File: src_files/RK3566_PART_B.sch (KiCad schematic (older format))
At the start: 1 part

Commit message: wifi module complete
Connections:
- net eMMC_D1_FLASH_D1: now also U?.B27 (EMMC_D1)
- net eMMC_D2_FLASH_D2: now also U?.B32 (EMMC_D2)
- net SDMMC1_D3: now reaches U?.1A20 (SDMMC1_D3)
- net I2S2_SDO_M0: now reaches U?.1B20 (I2S2_LRCK_TX_M0)
- net SDMMC1_D0: now reaches U?.1C19 (SDMMC1_D0)
- net UART1_RX_M0: now reaches U?.1C20 (UART1_RX_M0)
- net SDMMC1_D2: now reaches U?.1D18 (SDMMC1_D2)
- net I2S2_LRCK_TX_M0: now reaches U?.1D19 (I2S2_LRCK_TX_M0)
- net SDMMC1_D1: now reaches U?.1E18 (SDMMC1_D1)
- net WIFI_REG_ON_H_GPIO2_B1: now reaches U?.A35 (SDMMC1_PWREN)
- net BT_WAKE_HOST_H_GPIO2_C0: now reaches U?.A37 (I2S2_LRCK_RX_M0)
- net WIFI_WAKE_HOST_H_GPIO2_B2: now reaches U?.B34 (SDMMC1_DET)
- net SDMMC1_CMD: now reaches U?.B35 (SDMMC1_CMD)
- net HOST_WAKE_BT_H_GPIO2_C1: now reaches U?.B36 (I2S2_MCLK_M0)
- net SDMMC1_CLK: now reaches U?.B37 (SDMMC1_CLK)
- net CLK32K_OUT1_WIFI: now reaches U?.B38 (CLK32K_OUT1)
- net I2S2_SCLK_TX_M0: now reaches U?.C37 (I2S2_SCLK_TX_M0)
- net I2S2_SDI_M0: now reaches U?.D37 (I2S2_SDI_M0)
- net BT_REG_ON_H_GPIO2_B7: now reaches U?.D38 (I2S2_SCLK_RX_M0)
- net UART1_RTSn_M0: now reaches U?.F37 (UART1_RTSn_M0)
- net UART1_TX_M0: now reaches U?.F38 (UART1_TX_M0)
- net UART1_CTSn_M0: now reaches U?.G37 (UART1_CTSn_M0)
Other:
- note added: "RK3566 TO WIFI/BT MODULE"
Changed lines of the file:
@@
 $Descr A3 16535 11693
 encoding utf-8
-Sheet 6 7
+Sheet 5 8
 Title ""
 Date ""
@@
 Text HLabel 3750 2025 0    33   Input ~ 0
 eMMC_CMD_FLASH_WRn
+Wire Wire Line
+	4025 1275 3750 1275
+Wire Wire Line
+	3750 1375 4025 1375
+Text HLabel 8250 1175 2    39   Input ~ 0
+SDMMC1_D0
+Text HLabel 8250 1275 2    39   Input ~ 0
+SDMMC1_D1
+Text HLabel 8250 1375 2    39   Input ~ 0
+SDMMC1_D2
+Text HLabel 8250 1475 2    39   Input ~ 0
+SDMMC1_D3
+Text HLabel 8250 1625 2    39   Input ~ 0
+SDMMC1_CMD
+Text HLabel 8250 1725 2    39   Input ~ 0
+SDMMC1_CLK
+Text HLabel 8250 1875 2    39   Input ~ 0
+WIFI_REG_ON_H_GPIO2_B1
+Text HLabel 8250 1975 2    39   Input ~ 0
+WIFI_WAKE_HOST_H_GPIO2_B2
+Wire Wire Line
+	8075 1175 8250 1175
+Wire Wire Line
+	8075 1275 8250 1275
+Wire Wire Line
+	8075 1375 8250 1375
+Wire Wire Line
+	8075 1475 8250 1475
+Wire Wire Line
+	8075 1625 8250 1625
+Wire Wire Line
+	8075 1725 8250 1725
+Wire Wire Line
+	8075 1875 8250 1875
+Wire Wire Line
+	8075 1975 8250 1975
+Text HLabel 8250 2175 2    39   Input ~ 0
+UART1_RX_M0
+Wire Wire Line
+	8075 2175 8250 2175
+Text HLabel 8250 2275 2    39   Input ~ 0
+UART1_TX_M0
+Wire Wire Line
+	8075 2275 8250 2275
+Text HLabel 8250 2375 2    39   Input ~ 0
+UART1_RTSn_M0
+Wire Wire Line
+	8075 2375 8250 2375
+Text HLabel 8250 2475 2    39   Input ~ 0
+UART1_CTSn_M0
+Wire Wire Line
+	8075 2475 8250 2475
+Text HLabel 8250 2625 2    39   Input ~ 0
+BT_REG_ON_H_GPIO2_B7
+Wire Wire Line
+	8075 2625 8250 2625
+Text HLabel 8250 2725 2    39   Input ~ 0
+BT_WAKE_HOST_H_GPIO2_C0
+Wire Wire Line
+	8075 2725 8250 2725
+Text HLabel 8250 2825 2    39   Input ~ 0
+HOST_WAKE_BT_H_GPIO2_C1
+Wire Wire Line
+	8075 2825 8250 2825
+Text HLabel 8250 2975 2    39   Input ~ 0
+I2S2_SCLK_TX_M0
+Wire Wire Line
+	8075 2975 8250 2975
+Text HLabel 8250 3075 2    39   Input ~ 0
+I2S2_LRCK_TX_M0
+Wire Wire Line
+	8075 3075 8250 3075
+Text HLabel 8250 3175 2    39   Input ~ 0
+I2S2_SDO_M0
+Wire Wire Line
+	8075 3175 8250 3175
+Text HLabel 8250 3275 2    39   Input ~ 0
+I2S2_SDI_M0
+Wire Wire Line
+	8075 3275 8250 3275
+Text HLabel 8250 3475 2    39   Input ~ 0
+CLK32K_OUT1_WIFI
+Wire Wire Line
+	8075 3475 8250 3475
+Wire Notes Line
+	8050 1050 9425 1050
+Wire Notes Line
+	9425 1050 9425 1750
+Text Notes 9475 2850 1    50   ~ 10
+RK3566 TO WIFI/BT MODULE
+Wire Notes Line
+	8075 3550 9450 3550
+Wire Notes Line
+	9450 3550 9450 2850
 $EndSCHEMATC

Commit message: sata updated
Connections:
- net SATA1_RX-: now reaches U?.V37 (USB3_HOST1_SSRXn/SATA1_RXn)
- net SATA1_RX+: now reaches U?.V38 (USB3_HOST1_SSRXp/SATA1_RXp)
- net SATA1_TX+: now reaches U?.W37 (USB3_HOST1_SSTXp/SATA1_TXp)
- net SATA1_TX-: now reaches U?.W38 (USB3_HOST1_SSTXn/SATA1_TXn)
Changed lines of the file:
@@
 Wire Notes Line
 	9450 3550 9450 2850
+Text HLabel 3900 5275 0    30   Input ~ 0
+SATA1_TX+
+Text HLabel 3900 5375 0    30   Input ~ 0
+SATA1_TX-
+Wire Wire Line
+	4025 5275 3900 5275
+Wire Wire Line
+	3900 5375 4025 5375
+Text HLabel 3900 5525 0    30   Input ~ 0
+SATA1_RX+
+Text HLabel 3900 5625 0    30   Input ~ 0
+SATA1_RX-
+Wire Wire Line
+	4025 5525 3900 5525
+Wire Wire Line
+	3900 5625 4025 5625
 $EndSCHEMATC

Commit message: littleupdate
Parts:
- U1: renamed from U?; footprint (none) -> greencharge-footprints:BGA828C65P31X31_2100X2100X161N
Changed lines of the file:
@@
 $Descr A3 16535 11693
 encoding utf-8
-Sheet 5 11
+Sheet 4 11
 Title ""
 Date ""
@@
 P 6025 575
 AR Path="/62988BD1" Ref="U?"  Part="3"
-AR Path="/62987DE9/62988BD1" Ref="U?"  Part="3"
-F 0 "U?" H 6050 240 50  0000 C CNN
+AR Path="/62987DE9/62988BD1" Ref="U1"  Part="3"
+F 0 "U1" H 6050 240 50  0000 C CNN
 F 1 "RK3566" H 6050 149 50  0000 C CNN
-F 2 "" H 5475 475 50  0001 C CNN
+F 2 "greencharge-footprints:BGA828C65P31X31_2100X2100X161N" H 5475 475 50  0001 C CNN
 F 3 "" H 5475 475 50  0001 C CNN
 	3    6025 575

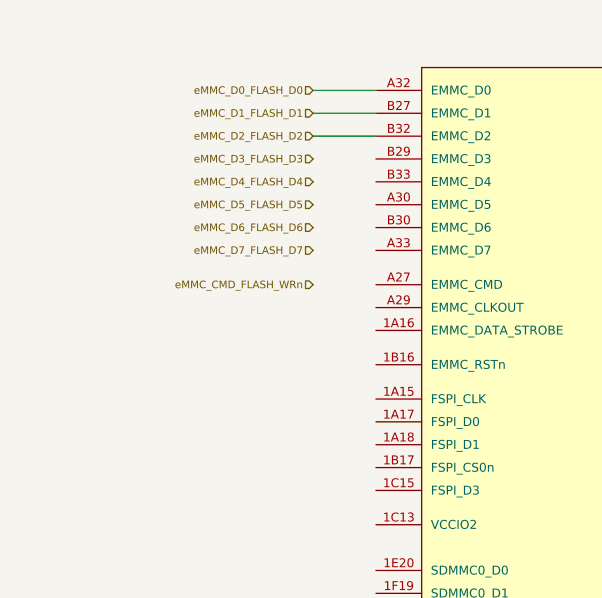
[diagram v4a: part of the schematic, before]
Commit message: added 3 screens
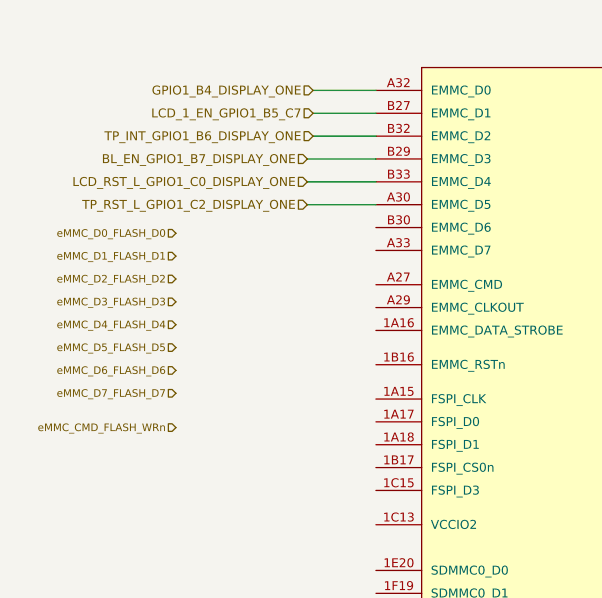
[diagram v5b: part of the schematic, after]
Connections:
- net eMMC_D0_FLASH_D0: no longer U1.A32 (EMMC_D0)
- net eMMC_D1_FLASH_D1: no longer U1.B27 (EMMC_D1)
- net eMMC_D2_FLASH_D2: no longer U1.B32 (EMMC_D2)
- net TP_RST_L_GPIO1_C2_DISPLAY_ONE: now reaches U1.A30 (EMMC_D5)
- net BL_EN_GPIO1_B7_DISPLAY_ONE: now reaches U1.B29 (EMMC_D3)
- net LCD_RST_L_GPIO1_C0_DISPLAY_ONE: now reaches U1.B33 (EMMC_D4)
- new net GPIO1_B4_DISPLAY_ONE: U1.A32 (EMMC_D0)
- new net LCD_1_EN_GPIO1_B5_C7: U1.B27 (EMMC_D1)
- new net TP_INT_GPIO1_B6_DISPLAY_ONE: U1.B32 (EMMC_D2)
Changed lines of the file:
@@
 	1    0    0    -1
 $EndComp
-Text HLabel 3750 1175 0    33   Input ~ 0
-eMMC_D0_FLASH_D0
-Wire Wire Line
-	4025 1175 3750 1175
-Text HLabel 3750 1275 0    33   Input ~ 0
-eMMC_D1_FLASH_D1
-Text HLabel 3750 1375 0    33   Input ~ 0
-eMMC_D2_FLASH_D2
-Text HLabel 3750 1475 0    33   Input ~ 0
-eMMC_D3_FLASH_D3
-Text HLabel 3750 1575 0    33   Input ~ 0
-eMMC_D4_FLASH_D4
-Text HLabel 3750 1675 0    33   Input ~ 0
-eMMC_D5_FLASH_D5
-Text HLabel 3750 1775 0    33   Input ~ 0
-eMMC_D6_FLASH_D6
-Text HLabel 3750 1875 0    33   Input ~ 0
-eMMC_D7_FLASH_D7
-Text HLabel 3750 2025 0    33   Input ~ 0
-eMMC_CMD_FLASH_WRn
-Wire Wire Line
-	4025 1275 3750 1275
-Wire Wire Line
-	3750 1375 4025 1375
 Text HLabel 8250 1175 2    39   Input ~ 0
 SDMMC1_D0
@@
 Wire Wire Line
 	3900 5625 4025 5625
+Wire Wire Line
+	3750 1375 4025 1375
+Wire Wire Line
+	4025 1275 3750 1275
+Text HLabel 3150 2650 0    33   Input ~ 0
+eMMC_CMD_FLASH_WRn
+Text HLabel 3150 2500 0    33   Input ~ 0
+eMMC_D7_FLASH_D7
+Text HLabel 3150 2400 0    33   Input ~ 0
+eMMC_D6_FLASH_D6
+Text HLabel 3150 2300 0    33   Input ~ 0
+eMMC_D5_FLASH_D5
+Text HLabel 3150 2200 0    33   Input ~ 0
+eMMC_D4_FLASH_D4
+Text HLabel 3150 2100 0    33   Input ~ 0
+eMMC_D3_FLASH_D3
+Text HLabel 3150 2000 0    33   Input ~ 0
+eMMC_D2_FLASH_D2
+Text HLabel 3150 1900 0    33   Input ~ 0
+eMMC_D1_FLASH_D1
+Wire Wire Line
+	4025 1175 3750 1175
+Text HLabel 3150 1800 0    33   Input ~ 0
+eMMC_D0_FLASH_D0
+Text HLabel 3750 1175 0    39   Input ~ 0
+GPIO1_B4_DISPLAY_ONE
+Text HLabel 3750 1275 0    39   Input ~ 0
+LCD_1_EN_GPIO1_B5_C7
+Text HLabel 3750 1375 0    39   Input ~ 0
+TP_INT_GPIO1_B6_DISPLAY_ONE
+Text HLabel 3725 1475 0    39   Input ~ 0
+BL_EN_GPIO1_B7_DISPLAY_ONE
+Wire Wire Line
+	4025 1475 3725 1475
+Text HLabel 3725 1575 0    39   Input ~ 0
+LCD_RST_L_GPIO1_C0_DISPLAY_ONE
+Text HLabel 3725 1675 0    39   Input ~ 0
+TP_RST_L_GPIO1_C2_DISPLAY_ONE
+Wire Wire Line
+	4025 1575 3725 1575
+Wire Wire Line
+	3725 1675 4025 1675
 $EndSCHEMATC

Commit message: all screens added_3 items left
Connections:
- net HDMITX_CEC_M0: now reaches U1.1V5 (HDMITX_CEC_M)
- net HDMITX_SDA: now reaches U1.AP11 (HDMITX_SDA)
- net HDMITX_SCL: now reaches U1.AR12 (HDMITX_SCL)
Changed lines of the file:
@@
 $Descr A3 16535 11693
 encoding utf-8
-Sheet 4 11
+Sheet 4 12
 Title ""
 Date ""
@@
 Comment4 ""
 $EndDescr
-$Comp
-L GCL_Integrated-Circuits:RK3566 U?
-U 3 1 62988BD1
-P 6025 575
-AR Path="/62988BD1" Ref="U?"  Part="3"
-AR Path="/62987DE9/62988BD1" Ref="U1"  Part="3"
-F 0 "U1" H 6050 240 50  0000 C CNN
-F 1 "RK3566" H 6050 149 50  0000 C CNN
-F 2 "greencharge-footprints:BGA828C65P31X31_2100X2100X161N" H 5475 475 50  0001 C CNN
-F 3 "" H 5475 475 50  0001 C CNN
-	3    6025 575
-	1    0    0    -1
-$EndComp
 Text HLabel 8250 1175 2    39   Input ~ 0
 SDMMC1_D0
@@
 Wire Wire Line
 	3725 1675 4025 1675
+Text HLabel 8325 4475 2    50   Input ~ 0
+HDMITX_CEC_M0
+$Comp
+L GCL_Integrated-Circuits:RK3566 U?
+U 3 1 62988BD1
+P 6025 575
+AR Path="/62988BD1" Ref="U?"  Part="3"
+AR Path="/62987DE9/62988BD1" Ref="U1"  Part="3"
+F 0 "U1" H 6050 240 50  0000 C CNN
+F 1 "RK3566" H 6050 149 50  0000 C CNN
+F 2 "greencharge-footprints:BGA828C65P31X31_2100X2100X161N" H 5475 475 50  0001 C CNN
+F 3 "" H 5475 475 50  0001 C CNN
+	3    6025 575
+	1    0    0    -1
+$EndComp
+Wire Wire Line
+	8075 4475 8325 4475
+Text HLabel 8325 4375 2    50   Input ~ 0
+HDMITX_SDA
+Text HLabel 8325 4275 2    50   Input ~ 0
+HDMITX_SCL
+Wire Wire Line
+	8075 4275 8325 4275
+Wire Wire Line
+	8075 4375 8325 4375
 $EndSCHEMATC

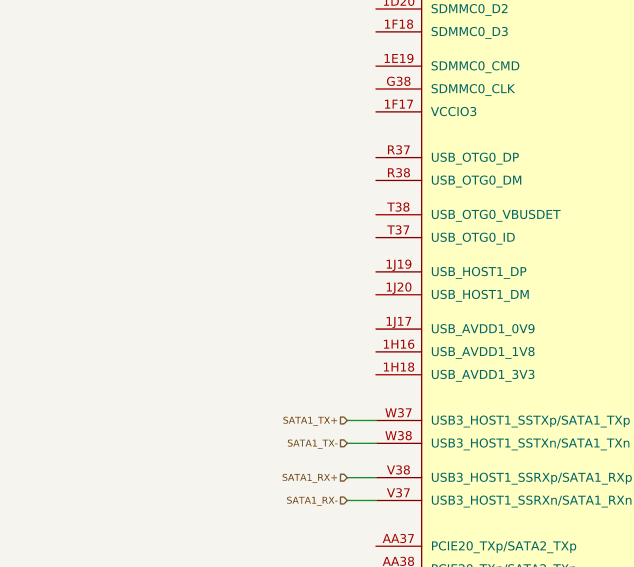
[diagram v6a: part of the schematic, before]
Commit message: updated 4G module and simcard
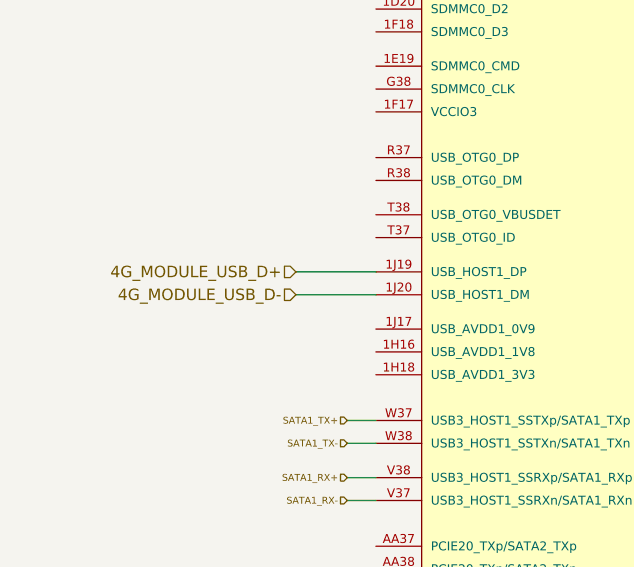
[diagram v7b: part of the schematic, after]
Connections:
- net 4G_MODULE_USB_D+: now reaches U1.1J19 (USB_HOST1_DP)
- net 4G_MODULE_USB_D-: now reaches U1.1J20 (USB_HOST1_DM)
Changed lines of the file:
@@
 $Descr A3 16535 11693
 encoding utf-8
-Sheet 4 12
+Sheet 4 13
 Title ""
 Date ""
@@
 Wire Wire Line
 	8075 4375 8325 4375
+Text HLabel 3675 4625 0    50   Input ~ 0
+4G_MODULE_USB_D+
+Text HLabel 3675 4725 0    50   Input ~ 0
+4G_MODULE_USB_D-
+Wire Wire Line
+	4025 4625 3675 4625
+Wire Wire Line
+	3675 4725 4025 4725
 $EndSCHEMATC

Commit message: update NFC, 5G, GPS__left LiPo charger+screen changes
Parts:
- added C?: 100nF, symbol Device:C_Small
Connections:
- net UART6_TX_M1: now reaches U1.1E20 (SDMMC0_D0)
- net VCCIO_SD: now reaches U1.1F17 (VCCIO3)
- net VCCIO_SD: now also C?.1
- net UART6_RX_M1: now reaches U1.1F19 (SDMMC0_D1)
- net I2C4_SDA_M0_TO_NFC_SCL: now reaches U1.AE2 (GPIO4_B3_d)
- net I2C4_SDA_M0_TO_NFC_SDA: now reaches U1.AF2 (GPIO4_B2_d)
- net GPIO4_B1_d_TO_NFC_REQ: now reaches U1.AG2 (GPIO4_B1_d)
- new net GND: C?.2
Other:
- note added: "SATA_INTERFACE\nZ=90 Ohms"
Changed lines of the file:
@@
 $Descr A3 16535 11693
 encoding utf-8
-Sheet 4 13
+Sheet 13 13
 Title ""
 Date ""
@@
 Wire Wire Line
 	4025 1275 3750 1275
-Text HLabel 3150 2650 0    33   Input ~ 0
-eMMC_CMD_FLASH_WRn
-Text HLabel 3150 2500 0    33   Input ~ 0
-eMMC_D7_FLASH_D7
-Text HLabel 3150 2400 0    33   Input ~ 0
-eMMC_D6_FLASH_D6
-Text HLabel 3150 2300 0    33   Input ~ 0
-eMMC_D5_FLASH_D5
-Text HLabel 3150 2200 0    33   Input ~ 0
-eMMC_D4_FLASH_D4
-Text HLabel 3150 2100 0    33   Input ~ 0
-eMMC_D3_FLASH_D3
-Text HLabel 3150 2000 0    33   Input ~ 0
-eMMC_D2_FLASH_D2
-Text HLabel 3150 1900 0    33   Input ~ 0
-eMMC_D1_FLASH_D1
 Wire Wire Line
 	4025 1175 3750 1175
-Text HLabel 3150 1800 0    33   Input ~ 0
-eMMC_D0_FLASH_D0
 Text HLabel 3750 1175 0    39   Input ~ 0
 GPIO1_B4_DISPLAY_ONE
@@
 Wire Wire Line
 	3675 4725 4025 4725
+Text HLabel 3850 3375 0    50   Input ~ 0
+UART6_RX_M1
+Text HLabel 3850 3275 0    50   Input ~ 0
+UART6_TX_M1
+Wire Wire Line
+	4025 3275 3850 3275
+Wire Wire Line
+	3850 3375 4025 3375
+Text GLabel 3100 3925 0    33   Input ~ 7
+VCCIO_SD
+Wire Wire Line
+	3100 3925 3175 3925
+$Comp
+L Device:C_Small C?
+U 1 1 65AF545B
+P 3175 4100
+F 0 "C?" H 3267 4146 50  0000 L CNN
+F 1 "100nF" H 3267 4055 50  0000 L CNN
+F 2 "" H 3175 4100 50  0001 C CNN
+F 3 "~" H 3175 4100 50  0001 C CNN
+	1    3175 4100
+	1    0    0    -1
+$EndComp
+Wire Wire Line
+	3175 4000 3175 3925
+Connection ~ 3175 3925
+Wire Wire Line
+	3175 3925 4025 3925
+$Comp
+L OLIMEX_Power:GND #PWR?
+U 1 1 65AF8D31
+P 3175 4250
+F 0 "#PWR?" H 3175 4000 50  0001 C CNN
+F 1 "GND" H 3180 4077 50  0000 C CNN
+F 2 "" H 3175 4250 60  0000 C CNN
+F 3 "" H 3175 4250 60  0000 C CNN
+	1    3175 4250
+	1    0    0    -1
+$EndComp
+Wire Wire Line
+	3175 4250 3175 4200
+Text Notes 3575 5275 3    33   ~ 0
+SATA_INTERFACE\nZ=90 Ohms
+Text HLabel 3775 8225 0    50   Input ~ 0
+I2C4_SDA_M0_TO_NFC_SDA
+Text HLabel 3775 8325 0    50   Input ~ 0
+I2C4_SDA_M0_TO_NFC_SCL
+Wire Wire Line
+	4025 8225 3775 8225
+Wire Wire Line
+	3775 8325 4025 8325
+Text HLabel 3775 8125 0    50   Input ~ 0
+GPIO4_B1_d_TO_NFC_REQ
+Wire Wire Line
+	4025 8125 3775 8125
 $EndSCHEMATC
